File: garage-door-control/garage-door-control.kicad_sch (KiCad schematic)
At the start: 0 parts

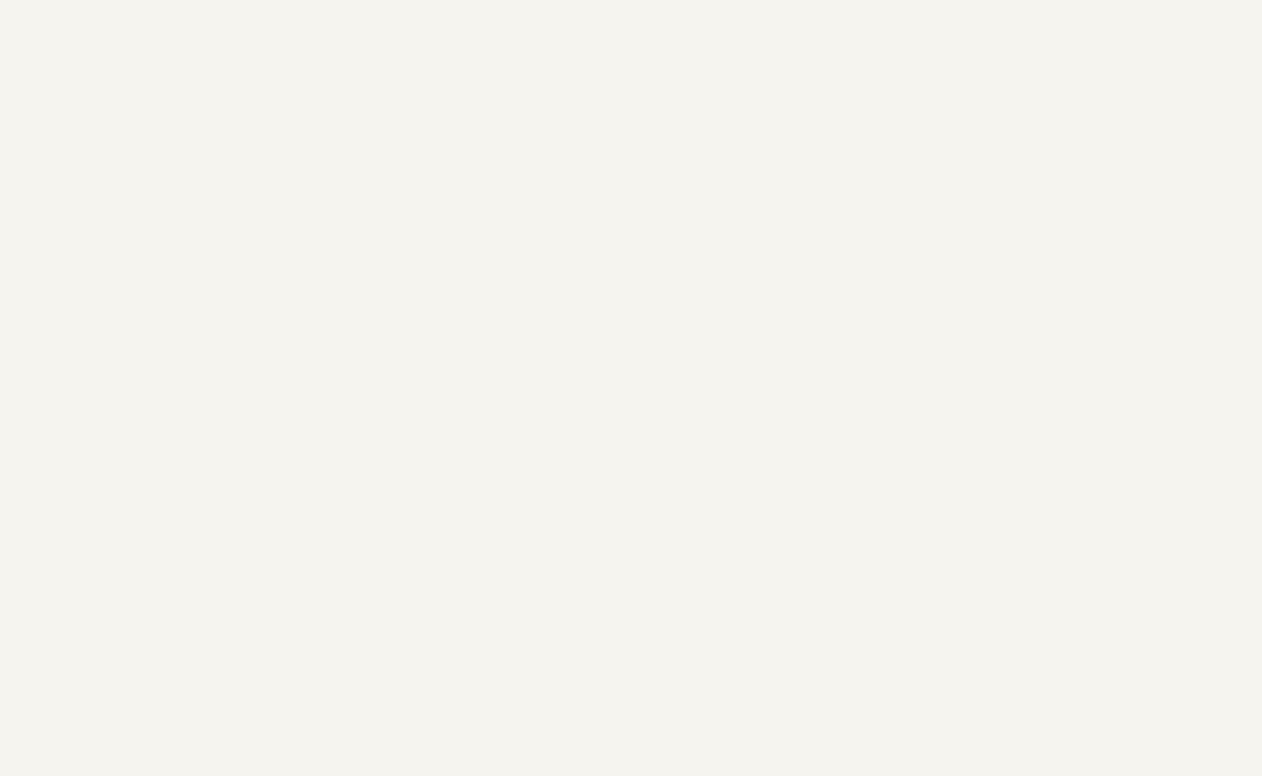
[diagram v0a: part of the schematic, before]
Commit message: Implement garage door control circuit diagram and mock board
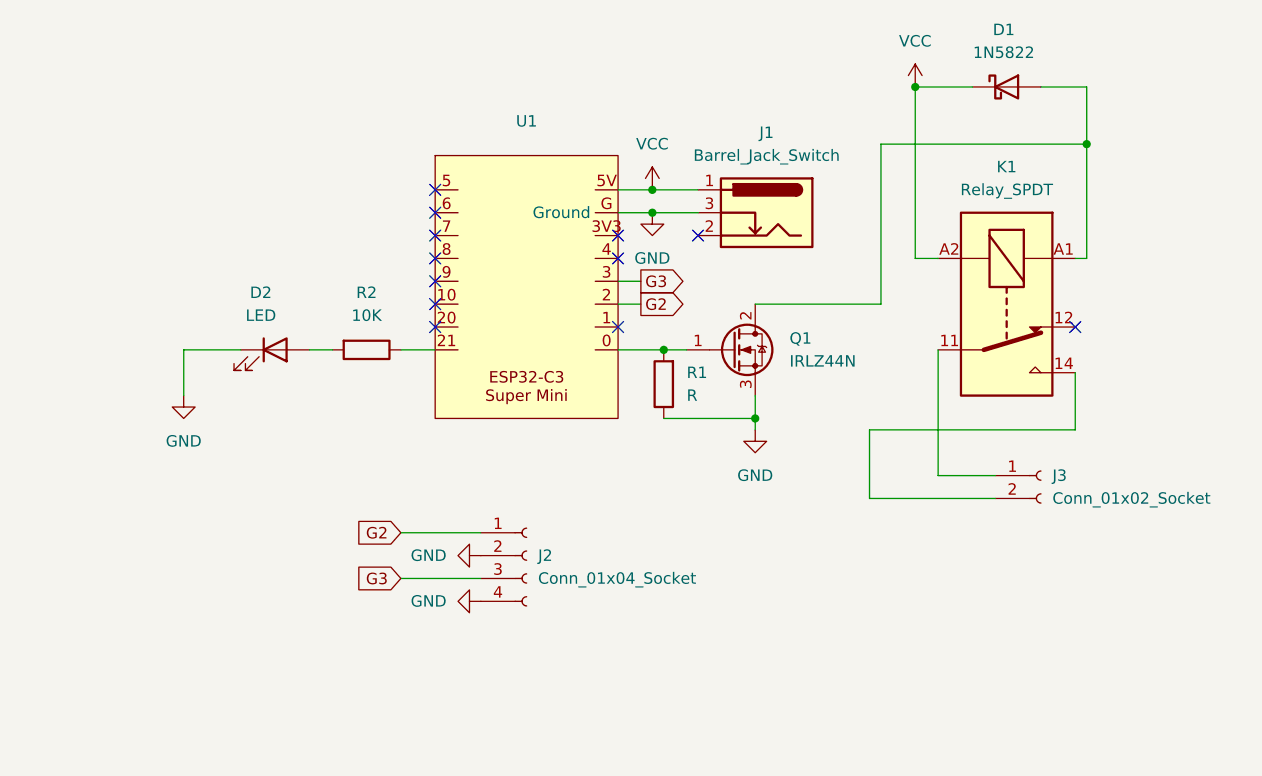
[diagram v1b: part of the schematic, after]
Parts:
- added D1: 1N5822, Diode_THT:D_DO-201AD_P15.24mm_Horizontal, symbol Diode:1N5822
- added D2: LED, custom:LED_0805_2012Metric_Pad1.15x1.40mm_HandSolder_simple, symbol Device:LED
- added J1: Barrel_Jack_Switch, Connector_BarrelJack:BarrelJack_CLIFF_FC681465S_SMT_Horizontal, symbol Connector:Barrel_Jack_Switch
- added J2: Conn_01x04_Socket, TerminalBlock_Phoenix:TerminalBlock_Phoenix_MKDS-1,5-4-5.08_1x04_P5.08mm_Horizontal, symbol Connector:Conn_01x04_Socket
- added J3: Conn_01x02_Socket, TerminalBlock_Phoenix:TerminalBlock_Phoenix_MKDS-1,5-2-5.08_1x02_P5.08mm_Horizontal, symbol Connector:Conn_01x02_Socket
- added K1: Relay_SPDT, Relay_THT:Relay_SPDT_Hongfa_HF3F-L-xx-1ZL1T, symbol Relay:Relay_SPDT
- added Q1: IRLZ44N, Package_TO_SOT_THT:TO-220-3_Vertical, symbol Transistor_FET:IRLZ44N
- added R1: R, Resistor_THT:R_Axial_DIN0204_L3.6mm_D1.6mm_P7.62mm_Horizontal, symbol Device:R
- added R2: 10K, Resistor_SMD:R_0805_2012Metric_Pad1.20x1.40mm_HandSolder, symbol Device:R
- added U1: ~, aliexpress:ESP32-C3-Super-Mini-Pins, symbol aliexpress:ESP32-C3-Super-Mini
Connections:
- net GND: now also D2.1 (K), J1.3, J2.2 (Pin_2), J2.4 (Pin_4), Q1.3 (S), R1.1, U1.G (Ground)
- net VCC: now also D1.1 (K), J1.1, K1.A2, U1.5V
- new net: D1.2 (A), K1.A1, Q1.2 (D)
- new net: Q1.1 (G), R1.2, U1.0
- new net: R2.1, U1.21
- new net: D2.2 (A), R2.2
- new net: J3.1 (Pin_1), K1.11
- new net: J3.2 (Pin_2), K1.14
- new net G2: J2.1 (Pin_1), U1.2
- new net G3: J2.3 (Pin_3), U1.3
- no-connect marks 0 -> 12

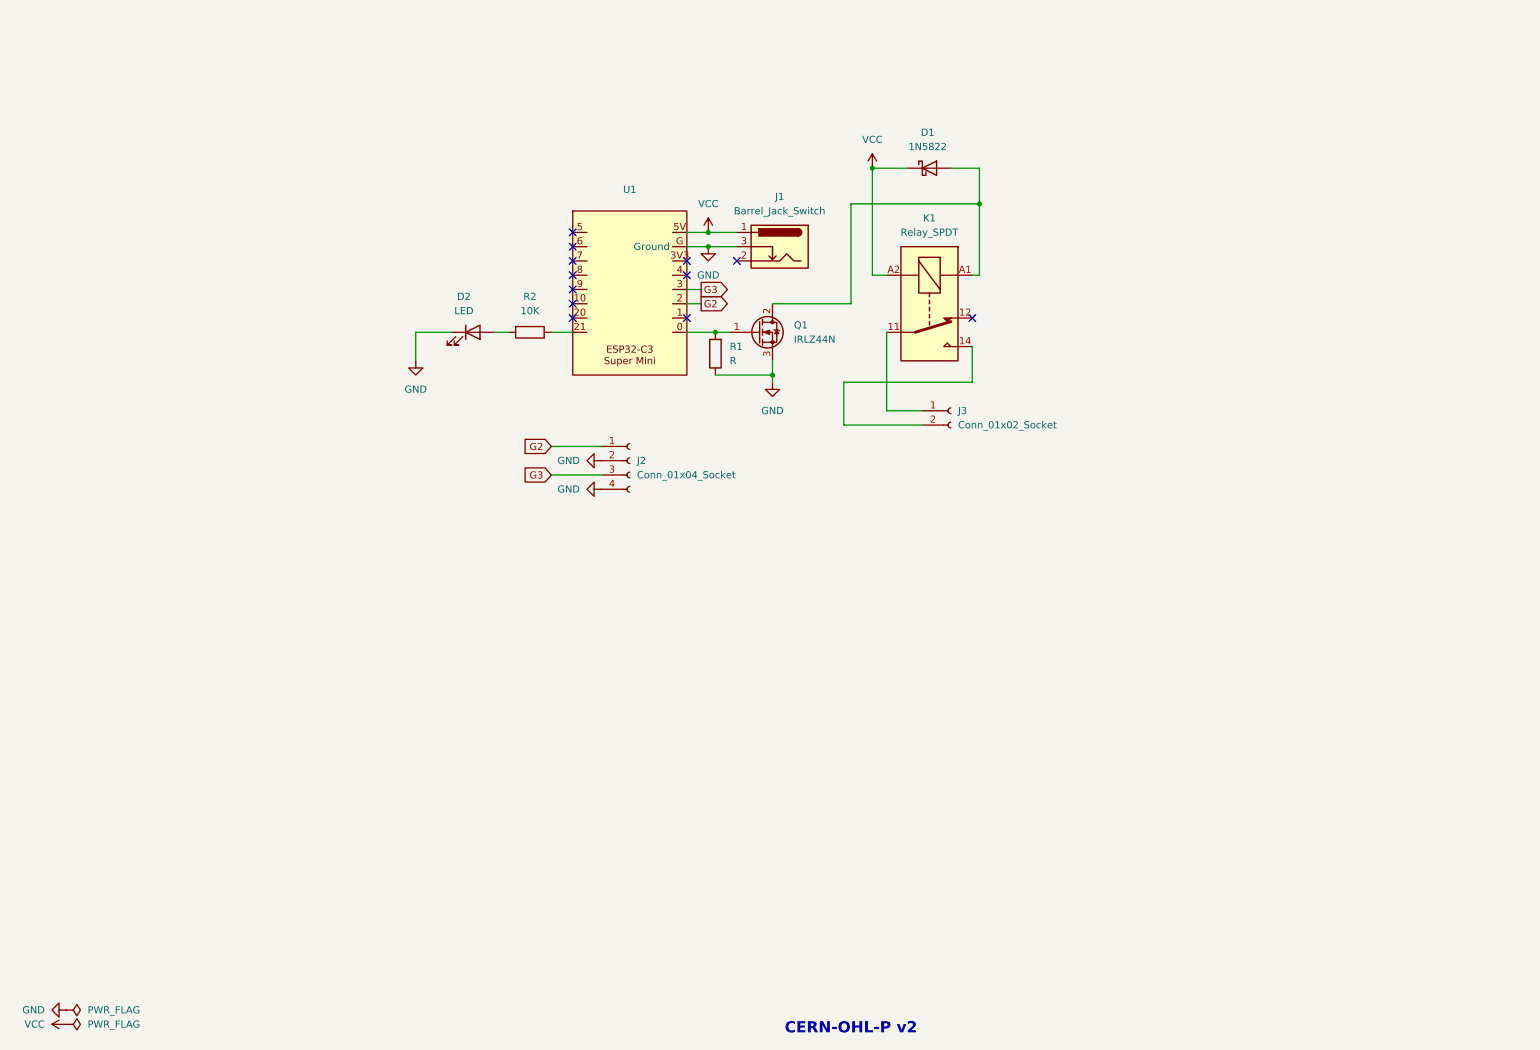
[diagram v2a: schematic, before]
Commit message: Rework garage board with sensors and for PCB printing
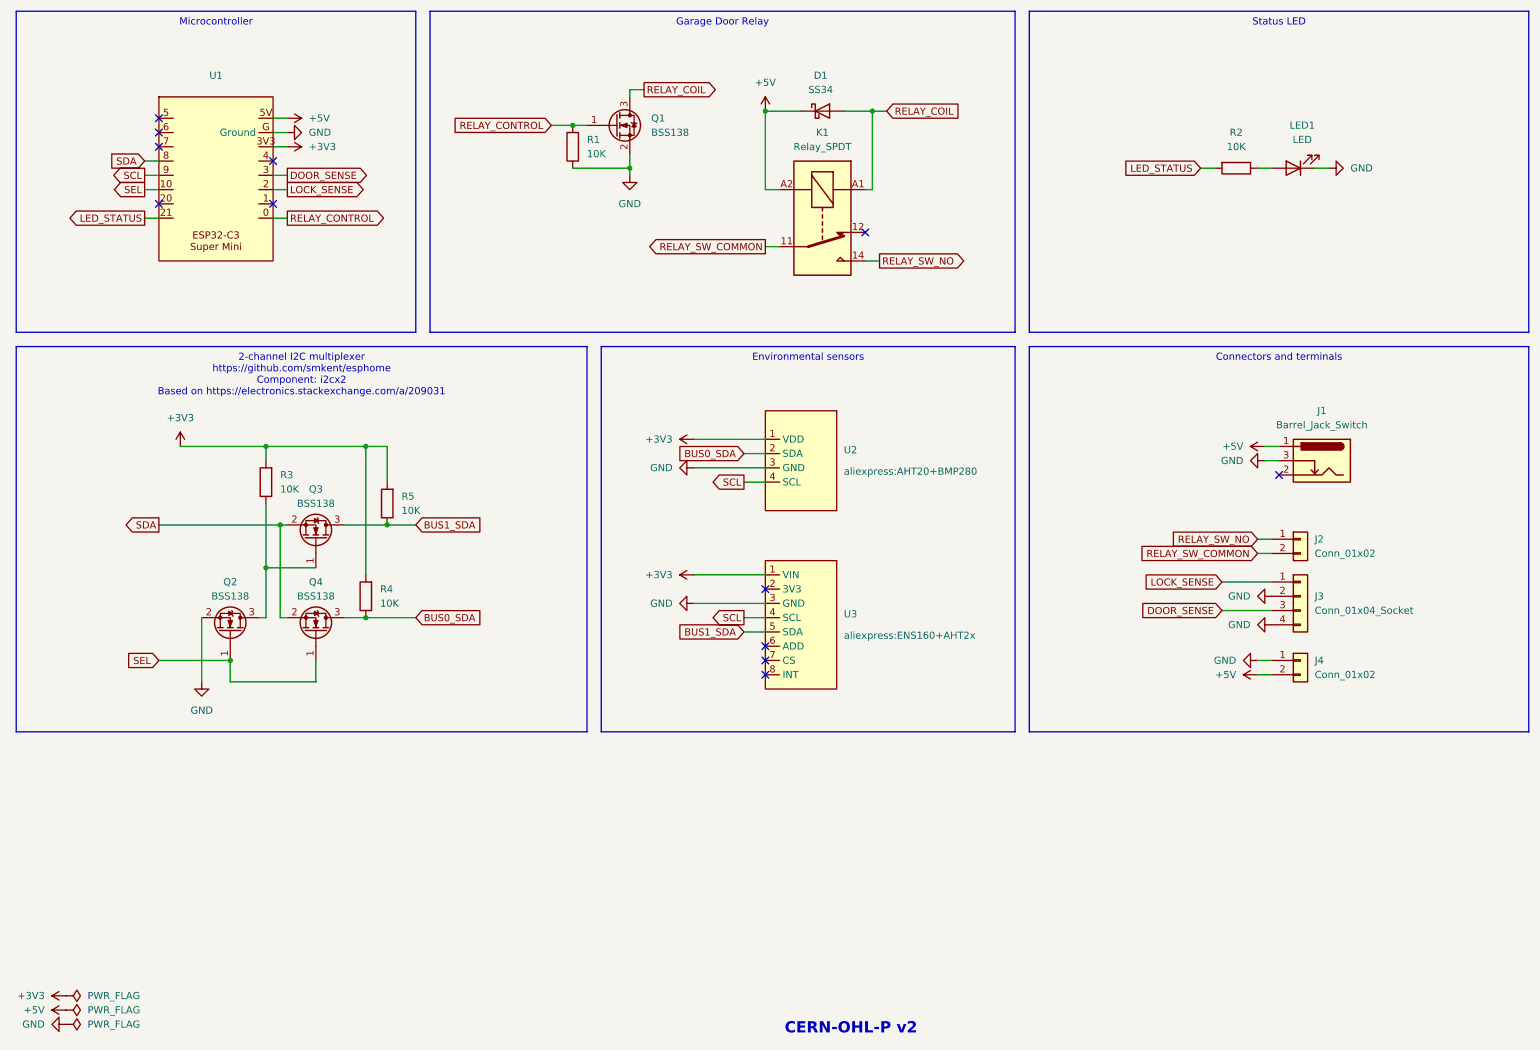
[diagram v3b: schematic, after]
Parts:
- removed D1: 1N5822, Diode_THT:D_DO-201AD_P15.24mm_Horizontal, symbol Diode:1N5822
- removed D2: LED, custom:LED_0805_2012Metric_Pad1.15x1.40mm_HandSolder_simple, symbol Device:LED
- removed J2: Conn_01x04_Socket, TerminalBlock_Phoenix:TerminalBlock_Phoenix_MKDS-1,5-4-5.08_1x04_P5.08mm_Horizontal, symbol Connector:Conn_01x04_Socket
- removed J3: Conn_01x02_Socket, TerminalBlock_Phoenix:TerminalBlock_Phoenix_MKDS-1,5-2-5.08_1x02_P5.08mm_Horizontal, symbol Connector:Conn_01x02_Socket
- removed Q1: IRLZ44N, Package_TO_SOT_THT:TO-220-3_Vertical, symbol Transistor_FET:IRLZ44N
- added D1: SS34, Diode_SMD:D_SMA, symbol Diode:SS34
- added J2: Conn_01x02, Connector_JST:JST_XH_B2B-XH-A_1x02_P2.50mm_Vertical, symbol Connector_Generic:Conn_01x02
- added J3: Conn_01x04_Socket, Connector_JST:JST_XH_B4B-XH-A_1x04_P2.50mm_Vertical, symbol Connector_Generic:Conn_01x04
- added J4: Conn_01x02, custom:TerminalBlock_Phoenix_MKDS-1,5-2-5.08_1x02_P5.08mm_Horizontal, symbol Connector_Generic:Conn_01x02
- added LED1: LED, custom:LED_0805_2012Metric_Pad1.15x1.40mm_HandSolder_simple, symbol Device:LED
- added Q1, Q2, Q3, Q4: BSS138, Package_TO_SOT_SMD:SOT-23, symbol Transistor_FET:BSS138
- added R3, R4, R5: 10K, Resistor_SMD:R_0805_2012Metric_Pad1.20x1.40mm_HandSolder, symbol Device:R
- added U2: ~, aliexpress:AHT20+BMP280, symbol aliexpress:AHT20+BMP280
- added U3: ~, aliexpress:ENS160+AHT2x, symbol aliexpress:ENS160+AHT2x
- R1: value R -> 10K; footprint Resistor_THT:R_Axial_DIN0204_L3.6mm_D1.6mm_P7.62mm_Horizontal -> Resistor_SMD:R_0805_2012Metric_Pad1.20x1.40mm_HandSolder
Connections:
- net GND: now also J3.2 (Pin_2), J3.4 (Pin_4), J4.1 (Pin_1), LED1.1 (K), Q1.2 (S), Q2.2 (S), U2.3 (GND), U3.3 (GND)
- net RELAY_COIL: now reaches K1.A1
- net RELAY_COIL: now also D1.2 (A), Q1.3 (D)
- net RELAY_CONTROL: now reaches R1.2, U1.0
- net RELAY_CONTROL: now also Q1.1 (G)
- net SEL: now reaches U1.10
- net SEL: now also Q2.1 (G), Q4.1 (G)
- net at R2.1: now also LED1.2 (A); no longer U1.21
- net +3V3: now reaches U1.3V3
- net +3V3: now also R3.2, R4.2, R5.2, U2.1 (VDD), U3.1 (VIN)
- net SDA: now reaches U1.8
- net SDA: now also Q3.2 (S), Q4.2 (S)
- net SCL: now reaches U1.9
- net SCL: now also U2.4 (SCL), U3.4 (SCL)
- net LED_STATUS: now reaches R2.2
- net LED_STATUS: now also U1.21
- net RELAY_SW_COMMON: now reaches K1.11
- net RELAY_SW_COMMON: now also J2.2 (Pin_2)
- net RELAY_SW_NO: now reaches K1.14
- net RELAY_SW_NO: now also J2.1 (Pin_1)
- net G2 renamed LOCK_SENSE
- net LOCK_SENSE: now also J3.1 (Pin_1)
- net G3 renamed DOOR_SENSE
- net DOOR_SENSE: now also J3.3 (Pin_3)
- net VCC renamed +5V
- net +5V: now also D1.1 (K), J4.2 (Pin_2)
- new net: Q2.3 (D), Q3.1 (G), R3.1
- new net BUS0_SDA: Q4.3 (D), R4.1, U2.2 (SDA)
- new net BUS1_SDA: Q3.3 (D), R5.1, U3.5 (SDA)
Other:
- moved on the sheet: K1, R1, U1

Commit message: Update Schottky diode PCB footprint
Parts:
- D1: footprint Diode_SMD:D_SMA -> custom:D_SMA_simple
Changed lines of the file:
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@@
 			)
 		)
-		(property "Footprint" "Diode_SMD:D_SMA"
+		(property "Footprint" "custom:D_SMA_simple"
 			(at 157.48 36.195 0)
 			(effects
